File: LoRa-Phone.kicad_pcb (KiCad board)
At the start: 4 copper layers, 81.6 x 102.5 mm, 218 parts, among them IC1 SKY13373-460LF, IC10 TPS22965NTDSGRQ1, IC2 AD8318ACPZ-REEL7, IC3 AD8318ACPZ-REEL7, IC4 TPS2121RUXT, IC5 MAX17048G+T10, IC6 MAX17048G+T10, IC7 TCA9543ADR, IC8 MAX16150AUT+T, IC9 SN74LVC1G74RSE2, J1 Interface, J3 Board_1, J4 BUTTON, J4 JST_MAIN, J5 Board_2, J6 ROTARY_ENCODER, M1 Motor_DC, Q1 AO3400A, Q2 AO3400A, Q3 AO3400A, Q4 AO3401A, SW1 POWER, U1 ESP32-S3-WROOM-2, U10 DRV2605LDGS, U11 LC76G, U12 RV-3028-C7, U13 SA818S, U14 INA219BxDCN, U15 INA219BxDCN, U16 INA219BxDCN, U17 MCP4725xxx-xCH, U18 TLV3501AIDBV, U19 RIC11-31S10K2-GSMT, U2 TCD-10-23BDX+, U21 WM8960, U23 E22-900M30S, U24 E22-170M30S, U3 MCP23017x-x-ML, U4 BMP390, U5 IS31FL3218-QF, U6 LSM6DSOXTR, U7 BQ24075RGT, U8 MCP23017x-x-ML, U9 BQ24075RGT

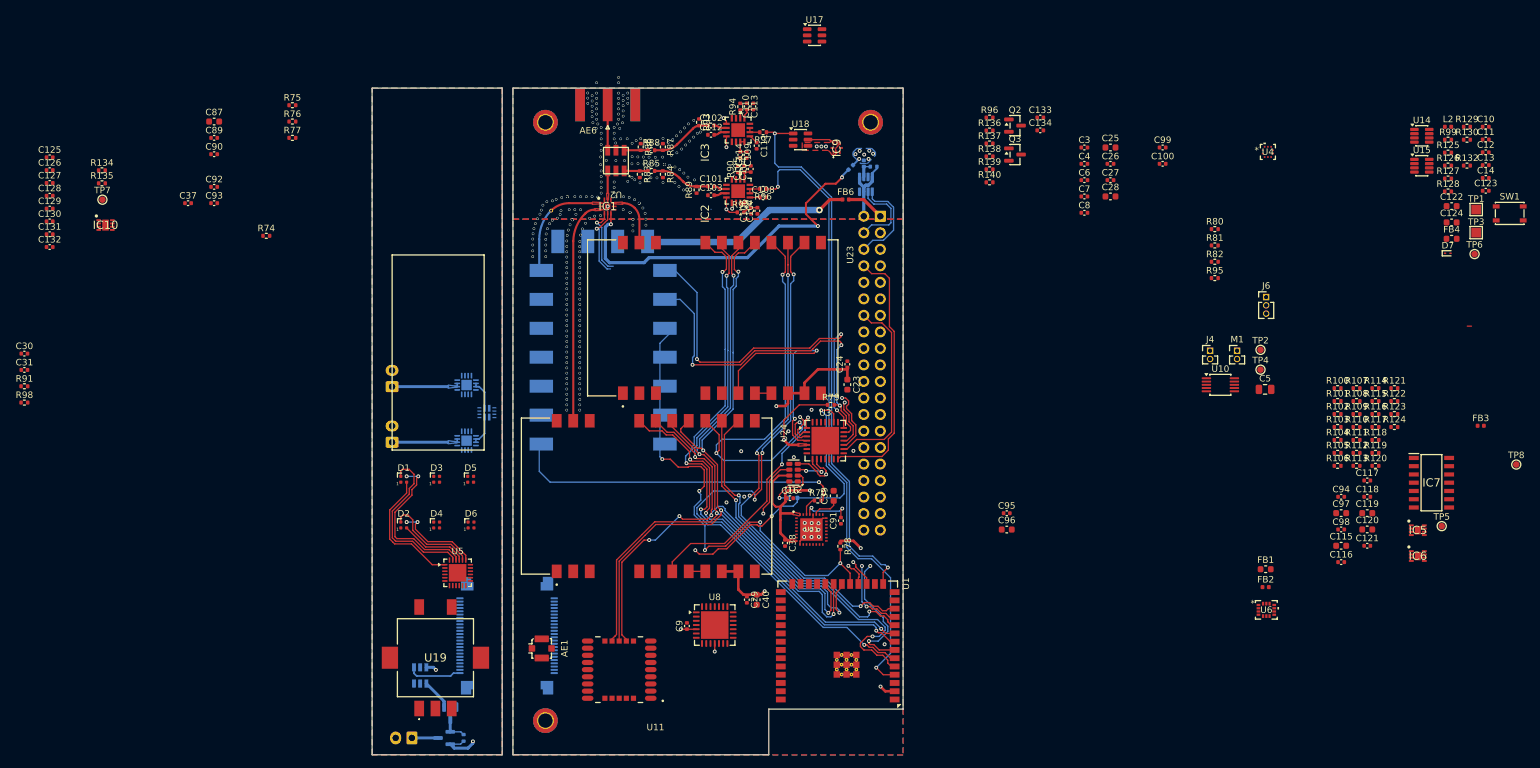
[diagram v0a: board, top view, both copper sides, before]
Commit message: Routed power section in the layout
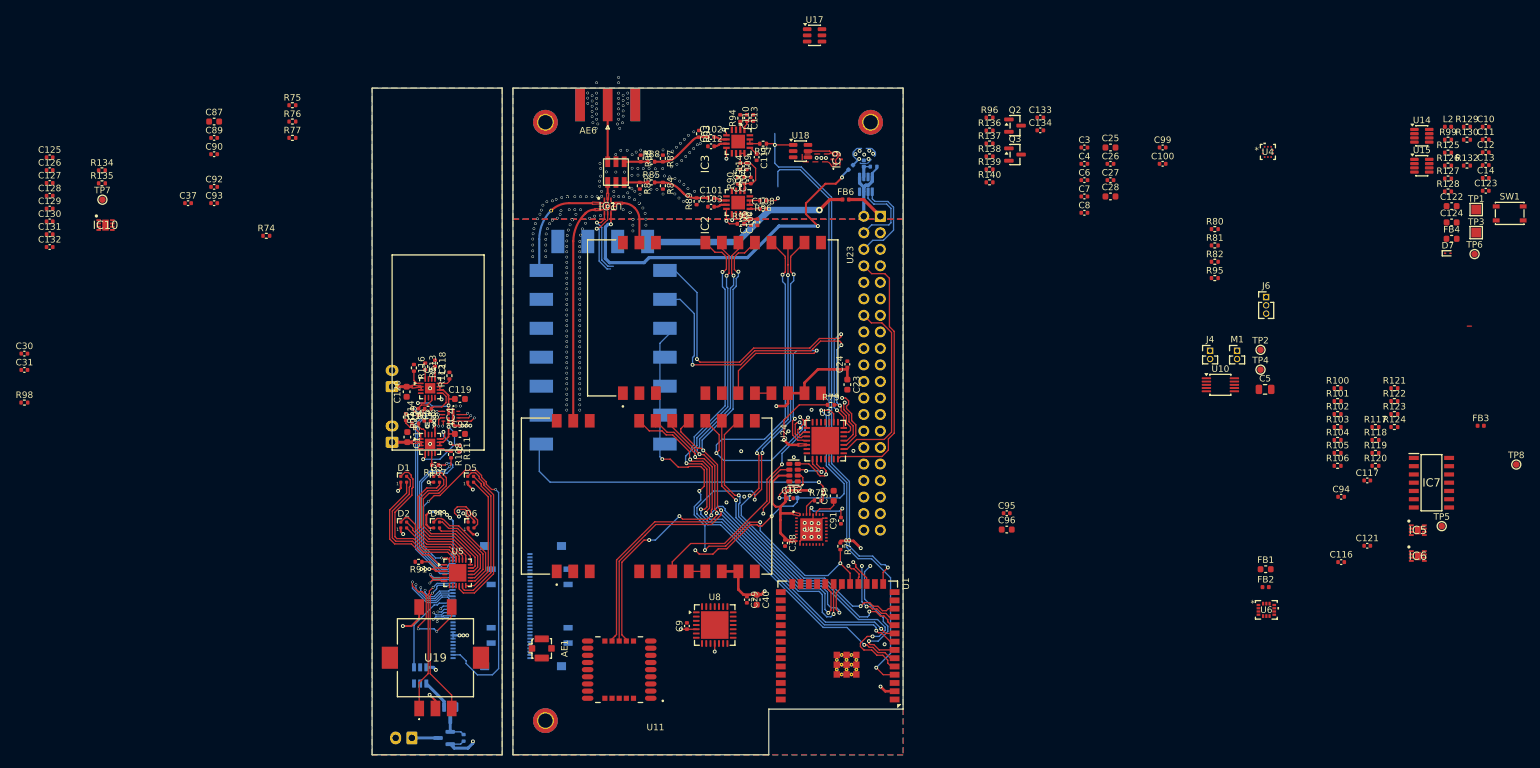
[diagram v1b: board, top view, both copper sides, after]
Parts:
- IC4, U7, U9: moved to F.Cu
- J3: footprint Connector_FFC-FPC:Amphenol_F32Q-1A7x1-11024_1x24-1MP_P0.5mm_Horizontal -> Connector_FFC-FPC:Molex_502244-3330_1x33-1MP_P0.5mm_Horizontal
- J5: value Board_2 -> Board_1; footprint Connector_FFC-FPC:Amphenol_F32Q-1A7x1-11024_1x24-1MP_P0.5mm_Horizontal -> Connector_FFC-FPC:Molex_502244-3330_1x33-1MP_P0.5mm_Horizontal
- moved C120 149.2 mm to (100.3, 97.9), turned to 90 degrees
- moved R116 148.0 mm to (101.4, 94.3), turned to -90 degrees
- moved R114 147.2 mm to (102.1, 101.0), turned to 90 degrees
- moved R109 146.1 mm to (100.2, 101.8), turned to -90 degrees
- moved R115 145.7 mm to (103.6, 100.5), turned to 180 degrees
- moved C118 144.8 mm to (104.6, 93.6), turned to -90 degrees
- moved R110 144.7 mm to (101.6, 102.8)
- moved C115 144.5 mm to (100.4, 104.9), turned to -90 degrees
- moved R113 144.0 mm to (103.1, 94.0), turned to -90 degrees
- moved R107 142.2 mm to (104.6, 109.2), turned to 180 degrees
- moved C98 141.5 mm to (103.5, 102.4)
- moved C119 140.6 mm to (108.5, 99.0)
- moved R112 140.0 mm to (106.8, 95.5), turned to 90 degrees
- moved R108 139.5 mm to (107.1, 107.6), turned to -90 degrees
- moved R111 137.9 mm to (108.4, 106.7), turned to -90 degrees
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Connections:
- J3 pad 1: POWER_BTN -> +3V3
- J3 pad 10: SHUTDOWN_1 -> ROT_ENC1
- J3 pad 11: BAT_VAL_1 -> ROT_ENC2
- J3 pad 12: BATS_RESET_1 -> JOYSTICK_X
- J3 pad 13: BATS_INT_1 -> JOYSTICK_Y
- J3 pad 14: +3V3 -> BUTTON1
- J3 pad 15: BAT1_PGOOD_1 -> BUTTON0
- J3 pad 16: BAT1_CHG_1 -> POWER_BTN
- J3 pad 17: BAT2_PGOOD_1 -> BATS_INT_1
- J3 pad 18: BAT2_CHG_1 -> BAT_SEL_1
- J3 pad 19: SDA -> SHUTDOWN_1
- J3 pad 2: GND -> +3V3
- J3 pad 20: JOYSTICK_X -> BAT_VAL_1
- J3 pad 21: JOYSTICK_Y -> BATS_RESET_1
- J3 pad 22: BUTTON1 -> GND
- J3 pad 23: +3V3 -> GND
- J3 pad 24: +3V3 -> GND
- J3 pad 3: GND -> +3V3
- J3 pad 4: GND -> BAT1_PGOOD_1
- J3 pad 5: BUTTON0 -> BAT1_CHG_1
- J3 pad 6: ROT_ENC1 -> BAT2_PGOOD_1
- J3 pad 7: ROT_ENC2 -> BAT2_CHG_1
- J3 pad 8: SCL -> SDA
- J3 pad 9: BAT_SEL_1 -> SCL
- J5 pad 10: BAT1_PGOOD -> ROT_ENC1_B
- J5 pad 11: +3V3 -> ROT_ENC2_B
- J5 pad 12: BATS_INT -> JOYSTICK_X_B
- J5 pad 13: BATS_RESET -> JOYSTICK_Y_B
- J5 pad 14: BAT_VAL -> BUTTON1_B
- J5 pad 15: SHUTDOWN -> BUTTON0_B
- J5 pad 16: BAT_SEL -> POWER_BTN_B
- J5 pad 17: SCL -> BATS_INT
- J5 pad 18: ROT_ENC2_B -> BAT_SEL
- J5 pad 19: ROT_ENC1_B -> SHUTDOWN
- J5 pad 20: BUTTON0_B -> BAT_VAL
- J5 pad 21: GND -> BATS_RESET
- J5 pad 24: POWER_BTN_B -> GND
- J5 pad 3: BUTTON1_B -> +3V3
- J5 pad 4: JOYSTICK_Y_B -> BAT1_PGOOD
- J5 pad 5: JOYSTICK_X_B -> BAT1_CHG
- J5 pad 6: SDA -> BAT2_PGOOD
- J5 pad 8: BAT2_PGOOD -> SDA_B
- J5 pad 9: BAT1_CHG -> SCL_B
- R98 pad 1: SDB -> SDB_1
- U3 pad 19: SDB -> SDB_1
- U5 pad 10: D5B -> D5G
- U5 pad 11: D5G -> D5B
- U5 pad 13: D4B -> D4G
- U5 pad 14: D4G -> D4B
- U5 pad 16: D3B -> D3G
- U5 pad 17: D3G -> D3B
- U5 pad 19: D2B -> D2G
- U5 pad 20: D2G -> D2B
- U5 pad 22: D1B -> D1G
- U5 pad 23: D1G -> D1B
- U5 pad 5: SDA -> SDA_B
- U5 pad 6: SCL -> SCL_B
- U5 pad 7: D6B -> D6G
- U5 pad 8: D6G -> D6B
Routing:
- net SDB: track 0.00 -> 62.6 mm, vias 0 -> 3
- net BAT2_PGOOD: track 0.00 -> 32.4 mm, vias 0 -> 1
- net +3V3: track 46.3 -> 77.8 mm, vias 16 -> 32
- net BAT2_CHG: track 0.00 -> 29.5 mm, vias 0 -> 1
- net D3G: track 0.00 -> 25.6 mm
- net BUTTON0_B: track 0.00 -> 25.4 mm, vias 0 -> 3
- net D5G: track 0.00 -> 25.4 mm
- net BAT1_PGOOD: track 0.00 -> 25.0 mm, vias 0 -> 1
- net BAT1_CHG: track 0.00 -> 23.8 mm, vias 0 -> 1
- net ROT_ENC2_B: track 0.00 -> 23.2 mm, vias 0 -> 1
- net D3B: track 0.00 -> 23.0 mm
- net ROT_ENC1_B: track 0.00 -> 22.8 mm, vias 0 -> 1
- net D5B: track 0.00 -> 22.0 mm
- net D3R: track 0.00 -> 20.5 mm
- net D5R: track 0.00 -> 19.0 mm
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- added copper zone on F.Cu, net BAT1
- added copper zone on F.Cu, net BAT2
- removed copper zone on B.Cu, net BAT1
- removed copper zone on B.Cu, net BAT2
